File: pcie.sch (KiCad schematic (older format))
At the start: 11 parts

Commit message: sch: Replace regular symbols with small variant
Done for most capacitors and resistors
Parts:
- removed C? (x8): 100n, symbol Device:C
- added C? (x8): 100n, symbol Device:C_Small
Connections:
- net PCIE_X4_RX0_N: now also C?.1
- net PCIE_X4_RX0_P: now also C?.1
- net PCIE_X4_RX1_N: now also C?.1
- net PCIE_X4_RX1_P: now also C?.1
- net PCIE_X4_RX2_N: now also C?.1
- net PCIE_X4_RX2_P: now also C?.1
- net PCIE_X4_RX3_N: now also C?.1
- net PCIE_X4_RX3_P: now also C?.1
- net X4_R0_N: now also C?.2
- net X4_R0_P: now also C?.2
- net X4_R1_N: now also C?.2
- net X4_R1_P: now also C?.2
- net X4_R2_N: now also C?.2
- net X4_R2_P: now also C?.2
- net X4_R3_N: now also C?.2
- net X4_R3_P: now also C?.2
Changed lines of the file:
@@
 PCIE_4X
 Wire Wire Line
-	9700 3500 10450 3500
-Wire Wire Line
-	9700 3600 10450 3600
+	9650 3500 10450 3500
+Wire Wire Line
+	9650 3600 10450 3600
 Text Label 10400 3500 2    50   ~ 0
 PCIE_X4_RX0_P
@@
 	7050 5000 7150 5100
 Wire Wire Line
-	9700 4400 10450 4400
-Wire Wire Line
-	9700 4500 10450 4500
+	9650 4400 10450 4400
+Wire Wire Line
+	9650 4500 10450 4500
 Text Label 10400 4400 2    50   ~ 0
 PCIE_X4_RX1_P
@@
 	10550 4400 10450 4500
 Wire Wire Line
-	9700 4800 10450 4800
-Wire Wire Line
-	9700 4900 10450 4900
+	9650 4800 10450 4800
+Wire Wire Line
+	9650 4900 10450 4900
 Text Label 10400 4800 2    50   ~ 0
 PCIE_X4_RX2_P
@@
 	10550 4800 10450 4900
 Wire Wire Line
-	9700 5200 10450 5200
-Wire Wire Line
-	9700 5300 10450 5300
+	9650 5200 10450 5200
+Wire Wire Line
+	9650 5300 10450 5300
 Text Label 10400 5200 2    50   ~ 0
 PCIE_X4_RX3_P
@@
 Text Label 9750 1600 2    50   ~ 0
 X4_PRSNT
-$Comp
-L Device:C C?
-U 1 1 5CBFD901
-P 9550 3500
-F 0 "C?" V 9500 3450 50  0000 R BNN
-F 1 "100n" V 9500 3550 50  0000 L BNN
-F 2 "" H 9588 3350 50  0001 C CNN
-F 3 "~" H 9550 3500 50  0001 C CNN
-	1    9550 3500
-	0    1    1    0
-$EndComp
-$Comp
-L Device:C C?
-U 1 1 5CBFD908
-P 9550 3600
-F 0 "C?" V 9600 3550 50  0000 R TNN
-F 1 "100n" V 9600 3650 50  0000 L TNN
-F 2 "" H 9588 3450 50  0001 C CNN
-F 3 "~" H 9550 3600 50  0001 C CNN
-	1    9550 3600
-	0    1    1    0
-$EndComp
-$Comp
-L Device:C C?
-U 1 1 5CC03E7D
-P 9550 4400
-F 0 "C?" V 9500 4350 50  0000 R BNN
-F 1 "100n" V 9500 4450 50  0000 L BNN
-F 2 "" H 9588 4250 50  0001 C CNN
-F 3 "~" H 9550 4400 50  0001 C CNN
-	1    9550 4400
-	0    1    1    0
-$EndComp
-$Comp
-L Device:C C?
-U 1 1 5CC03E84
-P 9550 4500
-F 0 "C?" V 9600 4450 50  0000 R TNN
-F 1 "100n" V 9600 4550 50  0000 L TNN
-F 2 "" H 9588 4350 50  0001 C CNN
-F 3 "~" H 9550 4500 50  0001 C CNN
-	1    9550 4500
-	0    1    1    0
-$EndComp
-$Comp
-L Device:C C?
-U 1 1 5CC0A2C7
-P 9550 4800
-F 0 "C?" V 9500 4750 50  0000 R BNN
-F 1 "100n" V 9500 4850 50  0000 L BNN
-F 2 "" H 9588 4650 50  0001 C CNN
-F 3 "~" H 9550 4800 50  0001 C CNN
-	1    9550 4800
-	0    1    1    0
-$EndComp
-$Comp
-L Device:C C?
-U 1 1 5CC0A2CE
-P 9550 4900
-F 0 "C?" V 9600 4850 50  0000 R TNN
-F 1 "100n" V 9600 4950 50  0000 L TNN
-F 2 "" H 9588 4750 50  0001 C CNN
-F 3 "~" H 9550 4900 50  0001 C CNN
-	1    9550 4900
-	0    1    1    0
-$EndComp
-$Comp
-L Device:C C?
-U 1 1 5CC1070F
-P 9550 5200
-F 0 "C?" V 9500 5150 50  0000 R BNN
-F 1 "100n" V 9500 5250 50  0000 L BNN
-F 2 "" H 9588 5050 50  0001 C CNN
-F 3 "~" H 9550 5200 50  0001 C CNN
-	1    9550 5200
-	0    1    1    0
-$EndComp
-$Comp
-L Device:C C?
-U 1 1 5CC10716
-P 9550 5300
-F 0 "C?" V 9600 5250 50  0000 R TNN
-F 1 "100n" V 9600 5350 50  0000 L TNN
-F 2 "" H 9588 5150 50  0001 C CNN
-F 3 "~" H 9550 5300 50  0001 C CNN
-	1    9550 5300
-	0    1    1    0
-$EndComp
-Wire Wire Line
-	8900 3500 9400 3500
-Wire Wire Line
-	9400 3600 8900 3600
-Wire Wire Line
-	8900 4400 9400 4400
-Wire Wire Line
-	9400 4500 8900 4500
-Wire Wire Line
-	8900 4800 9400 4800
-Wire Wire Line
-	9400 4900 8900 4900
-Wire Wire Line
-	8900 5200 9400 5200
-Wire Wire Line
-	9400 5300 8900 5300
+Wire Wire Line
+	8900 3500 9450 3500
+Wire Wire Line
+	9450 3600 8900 3600
+Wire Wire Line
+	8900 4400 9450 4400
+Wire Wire Line
+	9450 4500 8900 4500
+Wire Wire Line
+	8900 4800 9450 4800
+Wire Wire Line
+	9450 4900 8900 4900
+Wire Wire Line
+	8900 5200 9450 5200
+Wire Wire Line
+	9450 5300 8900 5300
 Text Label 9050 3500 0    50   ~ 0
 X4_R0_P
@@
 Text Notes 4200 5750 2    50   ~ 0
 PCIe switch to get 2 mini PCIe slots
+$Comp
+L Device:C_Small C?
+U 1 1 5D40DB7F
+P 9550 3600
+F 0 "C?" V 9650 3500 50  0000 C CNN
+F 1 "100n" V 9650 3750 50  0000 C CNN
+F 2 "" H 9550 3600 50  0001 C CNN
+F 3 "~" H 9550 3600 50  0001 C CNN
+	1    9550 3600
+	0    1    1    0
+$EndComp
+$Comp
+L Device:C_Small C?
+U 1 1 5D405D43
+P 9550 3500
+F 0 "C?" V 9450 3400 50  0000 C CNN
+F 1 "100n" V 9450 3650 50  0000 C CNN
+F 2 "" H 9550 3500 50  0001 C CNN
+F 3 "~" H 9550 3500 50  0001 C CNN
+	1    9550 3500
+	0    1    1    0
+$EndComp
+$Comp
+L Device:C_Small C?
+U 1 1 5D424E6B
+P 9550 4500
+F 0 "C?" V 9650 4400 50  0000 C CNN
+F 1 "100n" V 9650 4650 50  0000 C CNN
+F 2 "" H 9550 4500 50  0001 C CNN
+F 3 "~" H 9550 4500 50  0001 C CNN
+	1    9550 4500
+	0    1    1    0
+$EndComp
+$Comp
+L Device:C_Small C?
+U 1 1 5D424E71
+P 9550 4400
+F 0 "C?" V 9450 4300 50  0000 C CNN
+F 1 "100n" V 9450 4550 50  0000 C CNN
+F 2 "" H 9550 4400 50  0001 C CNN
+F 3 "~" H 9550 4400 50  0001 C CNN
+	1    9550 4400
+	0    1    1    0
+$EndComp
+$Comp
+L Device:C_Small C?
+U 1 1 5D431AA7
+P 9550 4900
+F 0 "C?" V 9650 4800 50  0000 C CNN
+F 1 "100n" V 9650 5050 50  0000 C CNN
+F 2 "" H 9550 4900 50  0001 C CNN
+F 3 "~" H 9550 4900 50  0001 C CNN
+	1    9550 4900
+	0    1    1    0
+$EndComp
+$Comp
+L Device:C_Small C?
+U 1 1 5D431AAD
+P 9550 4800
+F 0 "C?" V 9450 4700 50  0000 C CNN
+F 1 "100n" V 9450 4950 50  0000 C CNN
+F 2 "" H 9550 4800 50  0001 C CNN
+F 3 "~" H 9550 4800 50  0001 C CNN
+	1    9550 4800
+	0    1    1    0
+$EndComp
+$Comp
+L Device:C_Small C?
+U 1 1 5D43856C
+P 9550 5300
+F 0 "C?" V 9650 5200 50  0000 C CNN
+F 1 "100n" V 9650 5450 50  0000 C CNN
+F 2 "" H 9550 5300 50  0001 C CNN
+F 3 "~" H 9550 5300 50  0001 C CNN
+	1    9550 5300
+	0    1    1    0
+$EndComp
+$Comp
+L Device:C_Small C?
+U 1 1 5D438572
+P 9550 5200
+F 0 "C?" V 9450 5100 50  0000 C CNN
+F 1 "100n" V 9450 5350 50  0000 C CNN
+F 2 "" H 9550 5200 50  0001 C CNN
+F 3 "~" H 9550 5200 50  0001 C CNN
+	1    9550 5200
+	0    1    1    0
+$EndComp
 Wire Bus Line
 	1550 3200 1550 3700

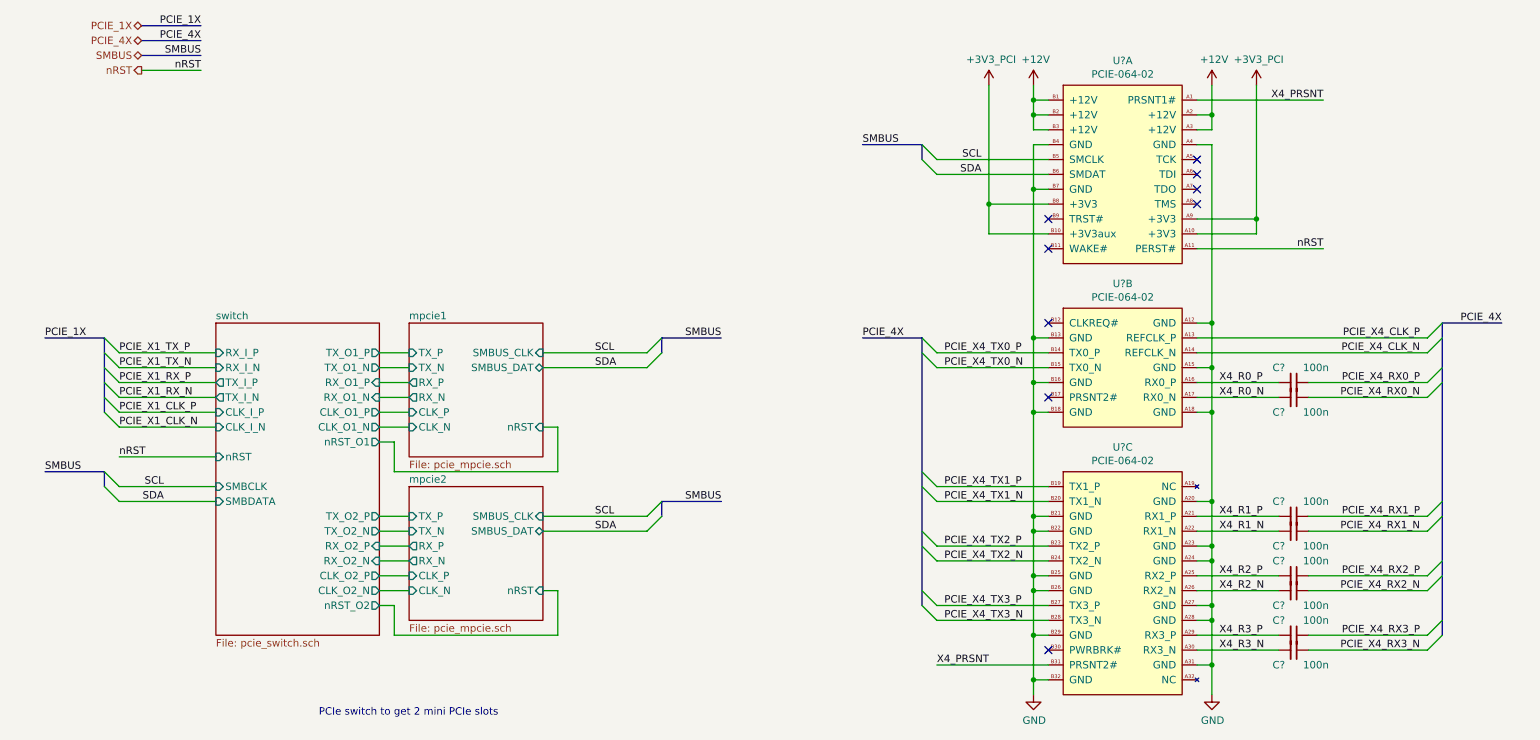
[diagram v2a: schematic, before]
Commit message: sch: Remove ALL busses since kicad's support is broken
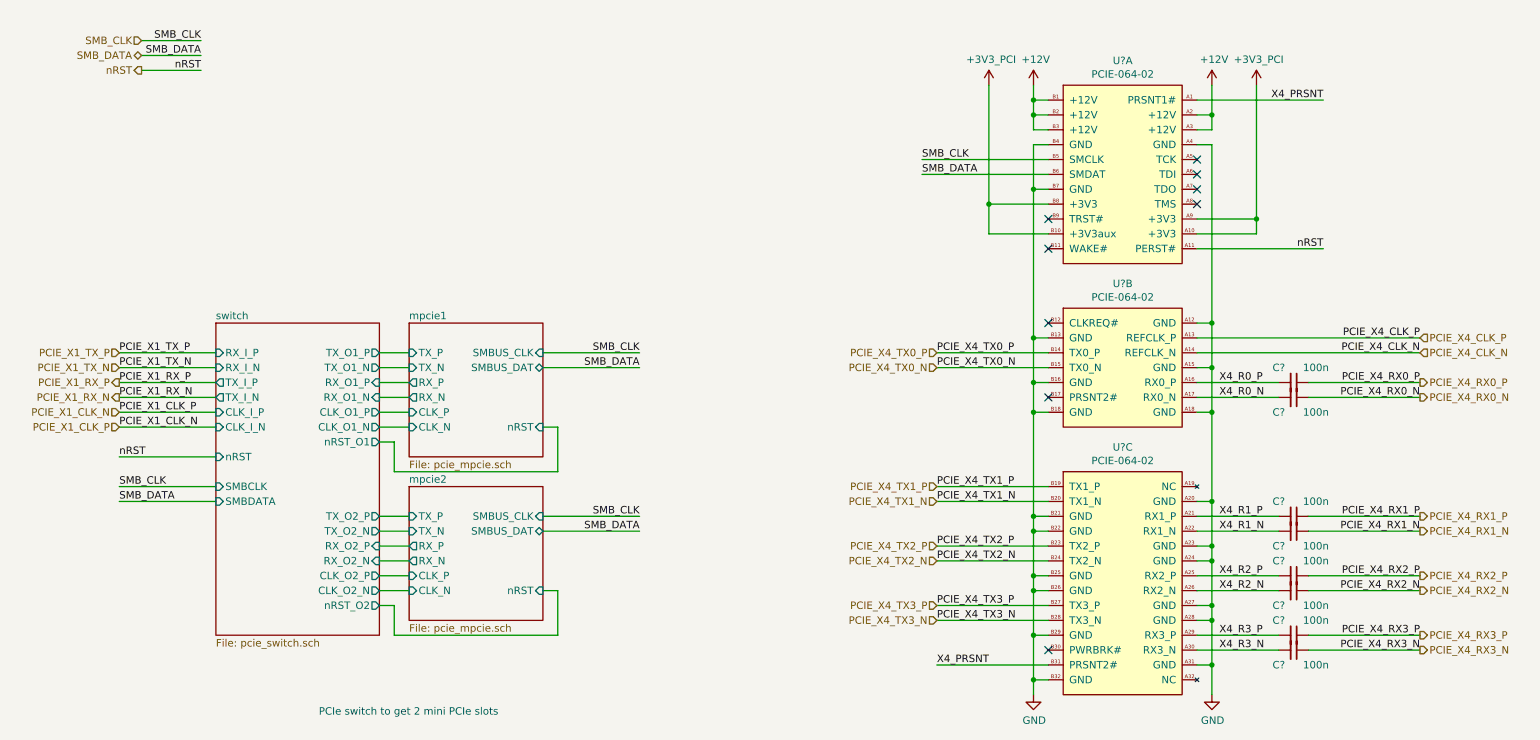
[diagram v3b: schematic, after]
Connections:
- net SCL renamed SMB_CLK
- net SDA renamed SMB_DATA

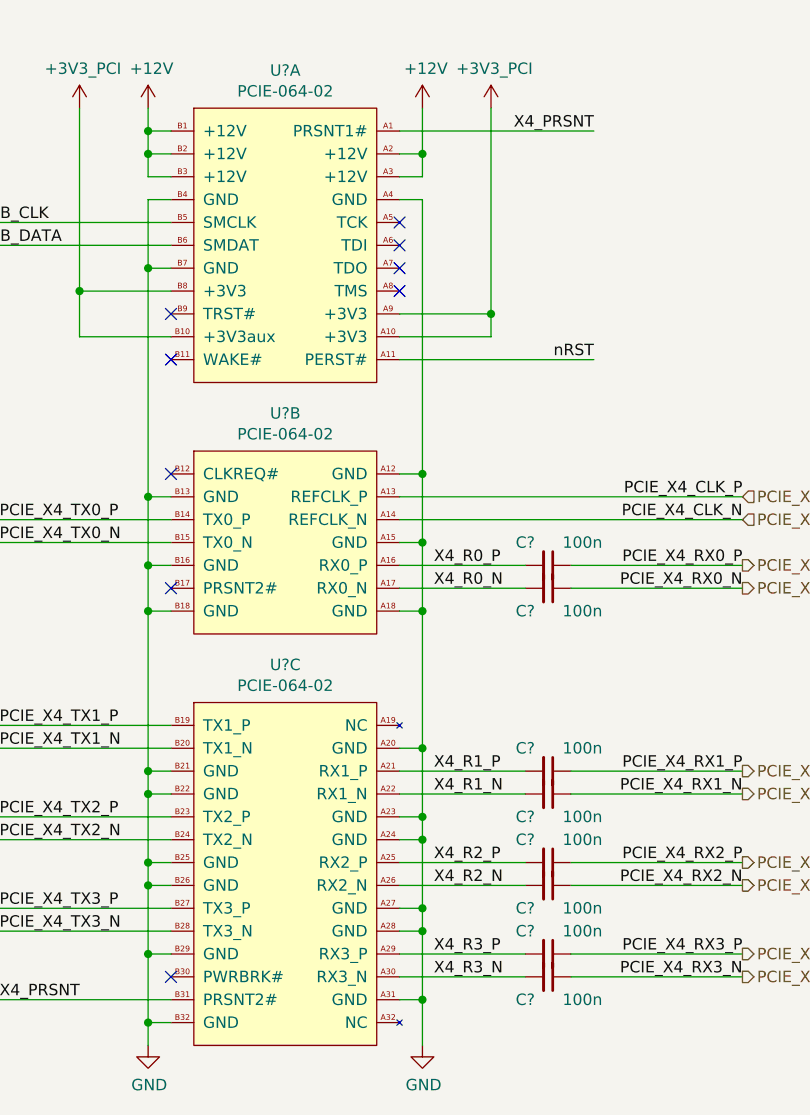
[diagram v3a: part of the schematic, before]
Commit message: sch: Annotate & associate symbols with footprints
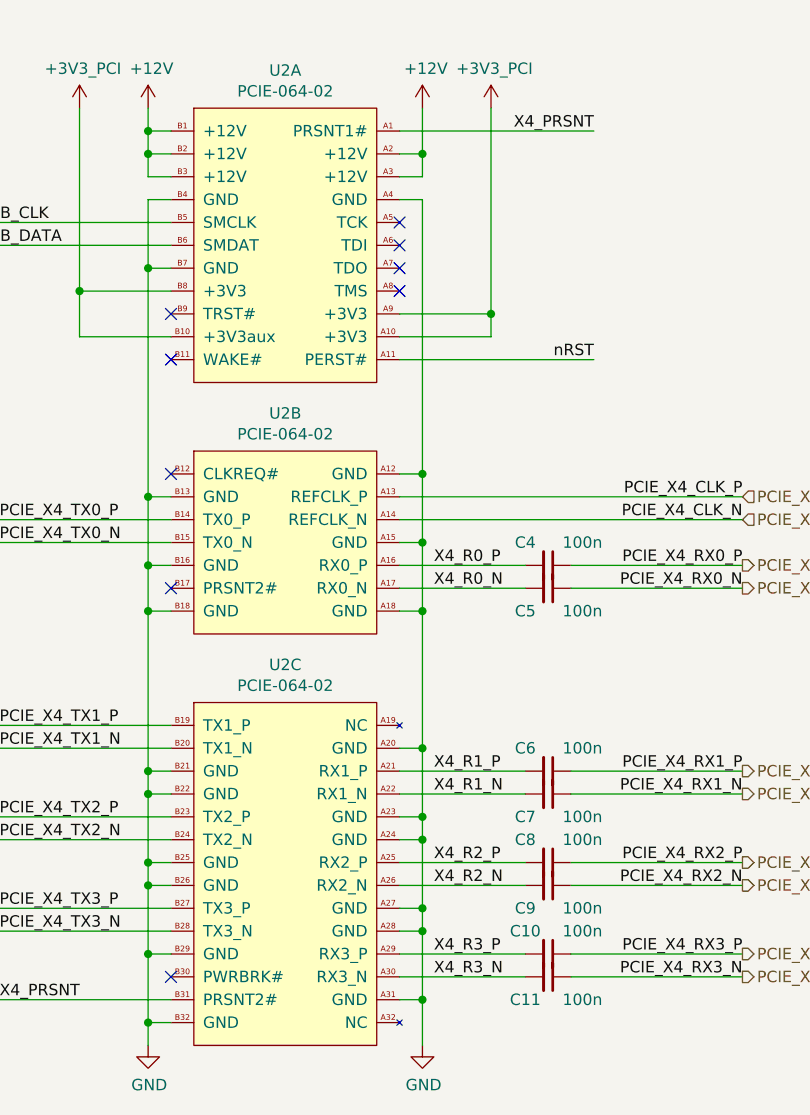
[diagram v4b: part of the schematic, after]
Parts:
- C10, C11, C4, C5, C6, C7, C8, C9: renamed from C?; footprint (none) -> Capacitor_SMD:C_0402_1005Metric
- U2: renamed from U?; footprint (none) -> pimouss-motherboard:SAMTEC_PCIE-064-02-F-D-TH
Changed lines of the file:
@@
 $EndDescr
 $Comp
-L pimouss-motherboard:PCIE-064-02 U?
+L pimouss-motherboard:PCIE-064-02 U2
 U 1 1 5C978539
 P 8000 1500
-F 0 "U?" H 8400 1665 50  0000 C CNN
+F 0 "U2" H 8400 1665 50  0000 C CNN
 F 1 "PCIE-064-02" H 8400 1574 50  0000 C CNN
-F 2 "" H 7900 1550 50  0001 C CNN
+F 2 "pimouss-motherboard:SAMTEC_PCIE-064-02-F-D-TH" H 7900 1550 50  0001 C CNN
 F 3 "" H 8000 1500 50  0001 C CNN
 	1    8000 1500
@@
 $EndComp
 $Comp
-L pimouss-motherboard:PCIE-064-02 U?
+L pimouss-motherboard:PCIE-064-02 U2
 U 2 1 5C978540
 P 8000 3000
-F 0 "U?" H 8400 3165 50  0000 C CNN
+F 0 "U2" H 8400 3165 50  0000 C CNN
 F 1 "PCIE-064-02" H 8400 3074 50  0000 C CNN
-F 2 "" H 7900 3050 50  0001 C CNN
+F 2 "pimouss-motherboard:SAMTEC_PCIE-064-02-F-D-TH" H 7900 3050 50  0001 C CNN
 F 3 "" H 8000 3000 50  0001 C CNN
 	2    8000 3000
@@
 $EndComp
 $Comp
-L pimouss-motherboard:PCIE-064-02 U?
+L pimouss-motherboard:PCIE-064-02 U2
 U 3 1 5C978547
 P 8000 4100
-F 0 "U?" H 8400 4265 50  0000 C CNN
+F 0 "U2" H 8400 4265 50  0000 C CNN
 F 1 "PCIE-064-02" H 8400 4174 50  0000 C CNN
-F 2 "" H 7900 4150 50  0001 C CNN
+F 2 "pimouss-motherboard:SAMTEC_PCIE-064-02-F-D-TH" H 7900 4150 50  0001 C CNN
 F 3 "" H 8000 4100 50  0001 C CNN
 	3    8000 4100
@@
 	9000 1900 9000 3100
 $Comp
-L power:GND #PWR?
+L power:GND #PWR030
 U 1 1 5C978552
 P 7800 5600
-F 0 "#PWR?" H 7800 5350 50  0001 C CNN
+F 0 "#PWR030" H 7800 5350 50  0001 C CNN
 F 1 "GND" H 7805 5427 50  0000 C CNN
 F 2 "" H 7800 5600 50  0001 C CNN
@@
 $EndComp
 $Comp
-L power:GND #PWR?
+L power:GND #PWR032
 U 1 1 5C978558
 P 9000 5600
-F 0 "#PWR?" H 9000 5350 50  0001 C CNN
+F 0 "#PWR032" H 9000 5350 50  0001 C CNN
 F 1 "GND" H 9005 5427 50  0000 C CNN
 F 2 "" H 9000 5600 50  0001 C CNN
@@
 	7500 2300 7500 1500
 $Comp
-L power:+12V #PWR?
+L power:+12V #PWR029
 U 1 1 5C9785A6
 P 7800 1500
-F 0 "#PWR?" H 7800 1350 50  0001 C CNN
+F 0 "#PWR029" H 7800 1350 50  0001 C CNN
 F 1 "+12V" H 7815 1673 50  0000 C CNN
 F 2 "" H 7800 1500 50  0001 C CNN
@@
 Connection ~ 7500 2300
 $Comp
-L power:+12V #PWR?
+L power:+12V #PWR031
 U 1 1 5C9785B5
 P 9000 1500
-F 0 "#PWR?" H 9000 1350 50  0001 C CNN
+F 0 "#PWR031" H 9000 1350 50  0001 C CNN
 F 1 "+12V" H 9015 1673 50  0000 C CNN
 F 2 "" H 9000 1500 50  0001 C CNN
@@
 	1800 1400 2200 1400
 $Comp
-L pimouss-motherboard:+3V3_PCI #PWR?
+L pimouss-motherboard:+3V3_PCI #PWR033
 U 1 1 5D1747BC
 P 9300 1500
-F 0 "#PWR?" H 9300 1350 50  0001 C CNN
+F 0 "#PWR033" H 9300 1350 50  0001 C CNN
 F 1 "+3V3_PCI" H 9315 1673 50  0000 C CNN
 F 2 "" H 9300 1500 50  0001 C CNN
@@
 $EndComp
 $Comp
-L pimouss-motherboard:+3V3_PCI #PWR?
+L pimouss-motherboard:+3V3_PCI #PWR028
 U 1 1 5D174907
 P 7500 1500
-F 0 "#PWR?" H 7500 1350 50  0001 C CNN
+F 0 "#PWR028" H 7500 1350 50  0001 C CNN
 F 1 "+3V3_PCI" H 7515 1673 50  0000 C CNN
 F 2 "" H 7500 1500 50  0001 C CNN
@@
 PCIe switch to get 2 mini PCIe slots
 $Comp
-L Device:C_Small C?
+L Device:C_Small C5
 U 1 1 5D40DB7F
 P 9550 3600
-F 0 "C?" V 9650 3500 50  0000 C CNN
+F 0 "C5" V 9650 3500 50  0000 C CNN
 F 1 "100n" V 9650 3750 50  0000 C CNN
-F 2 "" H 9550 3600 50  0001 C CNN
+F 2 "Capacitor_SMD:C_0402_1005Metric" H 9550 3600 50  0001 C CNN
 F 3 "~" H 9550 3600 50  0001 C CNN
 	1    9550 3600
@@
 $EndComp
 $Comp
-L Device:C_Small C?
+L Device:C_Small C4
 U 1 1 5D405D43
 P 9550 3500
-F 0 "C?" V 9450 3400 50  0000 C CNN
+F 0 "C4" V 9450 3400 50  0000 C CNN
 F 1 "100n" V 9450 3650 50  0000 C CNN
-F 2 "" H 9550 3500 50  0001 C CNN
+F 2 "Capacitor_SMD:C_0402_1005Metric" H 9550 3500 50  0001 C CNN
 F 3 "~" H 9550 3500 50  0001 C CNN
 	1    9550 3500
@@
 $EndComp
 $Comp
-L Device:C_Small C?
+L Device:C_Small C7
 U 1 1 5D424E6B
 P 9550 4500
-F 0 "C?" V 9650 4400 50  0000 C CNN
+F 0 "C7" V 9650 4400 50  0000 C CNN
 F 1 "100n" V 9650 4650 50  0000 C CNN
-F 2 "" H 9550 4500 50  0001 C CNN
+F 2 "Capacitor_SMD:C_0402_1005Metric" H 9550 4500 50  0001 C CNN
 F 3 "~" H 9550 4500 50  0001 C CNN
 	1    9550 4500
@@
 $EndComp
 $Comp
-L Device:C_Small C?
+L Device:C_Small C6
 U 1 1 5D424E71
 P 9550 4400
-F 0 "C?" V 9450 4300 50  0000 C CNN
+F 0 "C6" V 9450 4300 50  0000 C CNN
 F 1 "100n" V 9450 4550 50  0000 C CNN
-F 2 "" H 9550 4400 50  0001 C CNN
+F 2 "Capacitor_SMD:C_0402_1005Metric" H 9550 4400 50  0001 C CNN
 F 3 "~" H 9550 4400 50  0001 C CNN
 	1    9550 4400
@@
 $EndComp
 $Comp
-L Device:C_Small C?
+L Device:C_Small C9
 U 1 1 5D431AA7
 P 9550 4900
-F 0 "C?" V 9650 4800 50  0000 C CNN
+F 0 "C9" V 9650 4800 50  0000 C CNN
 F 1 "100n" V 9650 5050 50  0000 C CNN
-F 2 "" H 9550 4900 50  0001 C CNN
+F 2 "Capacitor_SMD:C_0402_1005Metric" H 9550 4900 50  0001 C CNN
 F 3 "~" H 9550 4900 50  0001 C CNN
 	1    9550 4900
@@
 $EndComp
 $Comp
-L Device:C_Small C?
+L Device:C_Small C8
 U 1 1 5D431AAD
 P 9550 4800
-F 0 "C?" V 9450 4700 50  0000 C CNN
+F 0 "C8" V 9450 4700 50  0000 C CNN
 F 1 "100n" V 9450 4950 50  0000 C CNN
-F 2 "" H 9550 4800 50  0001 C CNN
+F 2 "Capacitor_SMD:C_0402_1005Metric" H 9550 4800 50  0001 C CNN
 F 3 "~" H 9550 4800 50  0001 C CNN
 	1    9550 4800
@@
 $EndComp
 $Comp
-L Device:C_Small C?
+L Device:C_Small C11
 U 1 1 5D43856C
 P 9550 5300
-F 0 "C?" V 9650 5200 50  0000 C CNN
+F 0 "C11" V 9650 5200 50  0000 C CNN
 F 1 "100n" V 9650 5450 50  0000 C CNN
-F 2 "" H 9550 5300 50  0001 C CNN
+F 2 "Capacitor_SMD:C_0402_1005Metric" H 9550 5300 50  0001 C CNN
 F 3 "~" H 9550 5300 50  0001 C CNN
 	1    9550 5300
@@
 $EndComp
 $Comp
-L Device:C_Small C?
+L Device:C_Small C10
 U 1 1 5D438572
 P 9550 5200
-F 0 "C?" V 9450 5100 50  0000 C CNN
+F 0 "C10" V 9450 5100 50  0000 C CNN
 F 1 "100n" V 9450 5350 50  0000 C CNN
-F 2 "" H 9550 5200 50  0001 C CNN
+F 2 "Capacitor_SMD:C_0402_1005Metric" H 9550 5200 50  0001 C CNN
 F 3 "~" H 9550 5200 50  0001 C CNN
 	1    9550 5200
